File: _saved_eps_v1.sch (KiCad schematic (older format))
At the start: 8 parts

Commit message: Created netlist
Still missing deployment and RBL switches
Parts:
- removed U?: ATMEGA32M1-AU, TQFP32, symbol ATMEGA32M1-AU
- added C4, C5: 22pF, symbol C
- added U1: ATMEGA32M1-MU, QFN32, symbol ATMEGA32M1-MU
- added Y1: 8MHz, symbol Crystal_GND24
- gave numbers to parts that had none: 7
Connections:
- wire segments 16 -> 22
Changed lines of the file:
@@
 $EndDescr
 $Comp
-L switch S?
+L switch S1
 U 1 1 5998D4E2
 P 4700 4950
-F 0 "S?" H 4700 5100 60  0000 C CNN
+F 0 "S1" H 4700 5100 60  0000 C CNN
 F 1 "switch" H 4700 4900 60  0001 C CNN
 F 2 "" H 4700 4950 60  0001 C CNN
@@
 $EndComp
 $Comp
-L -BATT #PWR?
+L -BATT #PWR9
 U 1 1 5999015A
 P 4850 4950
-F 0 "#PWR?" H 4850 4800 50  0001 C CNN
+F 0 "#PWR9" H 4850 4800 50  0001 C CNN
 F 1 "-BATT" H 4850 5090 50  0000 C CNN
 F 2 "" H 4850 4950 50  0001 C CNN
@@
 $EndComp
 $Comp
-L switch S?
+L switch S2
 U 1 1 59990767
 P 4700 5400
-F 0 "S?" H 4700 5550 60  0000 C CNN
+F 0 "S2" H 4700 5550 60  0000 C CNN
 F 1 "switch" H 4700 5350 60  0001 C CNN
 F 2 "" H 4700 5400 60  0001 C CNN
@@
 $EndComp
 $Comp
-L switch S?
+L switch S3
 U 1 1 59990813
 P 4700 5750
-F 0 "S?" H 4700 5900 60  0000 C CNN
+F 0 "S3" H 4700 5900 60  0000 C CNN
 F 1 "switch" H 4700 5700 60  0001 C CNN
 F 2 "" H 4700 5750 60  0001 C CNN
@@
 $EndComp
 $Comp
-L +PACK #PWR?
+L +PACK #PWR5
 U 1 1 5999095F
 P 4550 5400
-F 0 "#PWR?" H 4550 5250 50  0001 C CNN
+F 0 "#PWR5" H 4550 5250 50  0001 C CNN
 F 1 "+PACK" H 4550 5540 50  0000 C CNN
 F 2 "" H 4550 5400 50  0001 C CNN
@@
 $EndComp
 $Comp
-L +BATT #PWR?
+L +BATT #PWR10
 U 1 1 599909D1
 P 4850 5750
-F 0 "#PWR?" H 4850 5600 50  0001 C CNN
+F 0 "#PWR10" H 4850 5600 50  0001 C CNN
 F 1 "+BATT" H 4850 5890 50  0000 C CNN
 F 2 "" H 4850 5750 50  0001 C CNN
@@
 $EndComp
 $Comp
-L switch S?
+L switch S4
 U 1 1 59990A70
 P 4750 4650
-F 0 "S?" H 4750 4800 60  0000 C CNN
+F 0 "S4" H 4750 4800 60  0000 C CNN
 F 1 "switch" H 4750 4600 60  0001 C CNN
 F 2 "" H 4750 4650 60  0001 C CNN
@@
 $EndComp
 $Comp
-L -PACK #PWR?
+L -PACK #PWR6
 U 1 1 59990B5A
 P 4600 4650
-F 0 "#PWR?" H 4600 4500 50  0001 C CNN
+F 0 "#PWR6" H 4600 4500 50  0001 C CNN
 F 1 "-PACK" H 4600 4790 50  0000 C CNN
 F 2 "" H 4600 4650 50  0001 C CNN
@@
 Text Notes 13600 1450 0    60   ~ 0
 Need to add the uC circuit (ATMEGA32M1)\nAdd all current and voltage sensors\ndecide whether to add the gas gauge (y) and the charging module (n)\nduplicate 3V3 supply and add a 12V supply
-$Comp
-L ATMEGA32M1-AU U?
-U 1 1 59D409BA
-P 6100 3000
-F 0 "U?" H 5150 4830 50  0000 L BNN
-F 1 "ATMEGA32M1-AU" H 6600 1600 50  0000 L BNN
-F 2 "TQFP32" H 6100 3000 50  0001 C CIN
-F 3 "" H 6100 3000 50  0001 C CNN
-	1    6100 3000
-	1    0    0    -1
-$EndComp
 $Sheet
 S 1550 6900 800  450
@@
 $EndSheet
 $Comp
-L GND #PWR?
+L GND #PWR11
 U 1 1 59EA5A22
 P 5000 4200
-F 0 "#PWR?" H 5000 3950 50  0001 C CNN
+F 0 "#PWR11" H 5000 3950 50  0001 C CNN
 F 1 "GND" H 5000 4050 50  0000 C CNN
 F 2 "" H 5000 4200 50  0001 C CNN
@@
 $EndComp
 $Comp
-L +3V3 #PWR?
+L +3V3 #PWR3
 U 1 1 59EA6A40
 P 4450 1300
-F 0 "#PWR?" H 4450 1150 50  0001 C CNN
+F 0 "#PWR3" H 4450 1150 50  0001 C CNN
 F 1 "+3V3" H 4450 1440 50  0000 C CNN
 F 2 "" H 4450 1300 50  0001 C CNN
@@
 $EndSheet
 $Sheet
-S 7850 3700 1000 1000
+S 8400 5100 1000 1000
 U 5A22FABC
 F0 "SWITCH_3V3" 60
 F1 "SWITCH_3V3.sch" 60
 $EndSheet
-Text HLabel 7850 3950 2    60   Input ~ 0
+Text HLabel 8400 5350 2    60   Input ~ 0
 3V3OUT
-Text HLabel 8850 3950 0    60   Output ~ 0
+Text HLabel 9400 5350 0    60   Output ~ 0
 N_3V3
-Text HLabel 7850 4200 2    60   Input ~ 0
+Text HLabel 8400 5600 2    60   Input ~ 0
 3V3_SWITCH
 $Sheet
@@
 Text HLabel 10650 2800 0    60   Output ~ 0
 E_9V
-Text HLabel 8850 4200 0    60   Output ~ 0
+Text HLabel 9400 5600 0    60   Output ~ 0
 E_3V3
 Text HLabel 9700 4850 2    60   Input ~ 0
@@
 Connection ~ 4750 1300
 $Comp
-L C C?
+L C C2
 U 1 1 5A75F62F
 P 4750 1050
-F 0 "C?" H 4775 1150 50  0000 L CNN
+F 0 "C2" H 4775 1150 50  0000 L CNN
 F 1 "0.1µF" H 4775 950 50  0000 L CNN
 F 2 "" H 4788 900 50  0001 C CNN
@@
 $EndComp
 $Comp
-L GND #PWR?
+L GND #PWR7
 U 1 1 5A75F783
 P 4750 900
-F 0 "#PWR?" H 4750 650 50  0001 C CNN
+F 0 "#PWR7" H 4750 650 50  0001 C CNN
 F 1 "GND" H 4750 750 50  0000 C CNN
 F 2 "" H 4750 900 50  0001 C CNN
@@
 $EndComp
 $Comp
-L +3V3 #PWR?
+L +3V3 #PWR1
 U 1 1 5A75F86F
 P 3600 1600
-F 0 "#PWR?" H 3600 1450 50  0001 C CNN
+F 0 "#PWR1" H 3600 1450 50  0001 C CNN
 F 1 "+3V3" H 3600 1740 50  0000 C CNN
 F 2 "" H 3600 1600 50  0001 C CNN
@@
 Connection ~ 3900 1600
 $Comp
-L C C?
+L C C1
 U 1 1 5A75F878
 P 3900 1350
-F 0 "C?" H 3925 1450 50  0000 L CNN
+F 0 "C1" H 3925 1450 50  0000 L CNN
 F 1 "0.1µF" H 3925 1250 50  0000 L CNN
 F 2 "" H 3938 1200 50  0001 C CNN
@@
 $EndComp
 $Comp
-L GND #PWR?
+L GND #PWR2
 U 1 1 5A75F87F
 P 3900 1200
-F 0 "#PWR?" H 3900 950 50  0001 C CNN
+F 0 "#PWR2" H 3900 950 50  0001 C CNN
 F 1 "GND" H 3900 1050 50  0000 C CNN
 F 2 "" H 3900 1200 50  0001 C CNN
@@
 $EndComp
 $Comp
-L +3V3 #PWR?
+L +3V3 #PWR4
 U 1 1 5A75F9CA
 P 4450 2000
-F 0 "#PWR?" H 4450 1850 50  0001 C CNN
+F 0 "#PWR4" H 4450 1850 50  0001 C CNN
 F 1 "+3V3" H 4450 2140 50  0000 C CNN
 F 2 "" H 4450 2000 50  0001 C CNN
@@
 Connection ~ 4750 2000
 $Comp
-L C C?
+L C C3
 U 1 1 5A75F9D3
 P 4750 2250
-F 0 "C?" H 4775 2350 50  0000 L CNN
+F 0 "C3" H 4775 2350 50  0000 L CNN
 F 1 "0.1µF" H 4775 2150 50  0000 L CNN
 F 2 "" H 4788 2100 50  0001 C CNN
@@
 $EndComp
 $Comp
-L GND #PWR?
+L GND #PWR8
 U 1 1 5A75F9DA
 P 4750 2400
-F 0 "#PWR?" H 4750 2150 50  0001 C CNN
+F 0 "#PWR8" H 4750 2150 50  0001 C CNN
 F 1 "GND" H 4750 2250 50  0000 C CNN
 F 2 "" H 4750 2400 50  0001 C CNN
@@
 	1    0    0    -1
 $EndComp
+$Comp
+L Crystal_GND24 Y1
+U 1 1 5A760437
+P 7850 4150
+F 0 "Y1" H 7975 4350 50  0000 L CNN
+F 1 "8MHz" H 7975 4275 50  0000 L CNN
+F 2 "" H 7850 4150 50  0001 C CNN
+F 3 "" H 7850 4150 50  0001 C CNN
+	1    7850 4150
+	0    1    1    0
+$EndComp
+Wire Wire Line
+	7400 4000 8400 4000
+Wire Wire Line
+	7400 4300 8400 4300
+$Comp
+L GND #PWR12
+U 1 1 5A7608B0
+P 7650 4150
+F 0 "#PWR12" H 7650 3900 50  0001 C CNN
+F 1 "GND" H 7650 4000 50  0000 C CNN
+F 2 "" H 7650 4150 50  0001 C CNN
+F 3 "" H 7650 4150 50  0001 C CNN
+	1    7650 4150
+	0    1    1    0
+$EndComp
+$Comp
+L GND #PWR13
+U 1 1 5A760948
+P 8050 4150
+F 0 "#PWR13" H 8050 3900 50  0001 C CNN
+F 1 "GND" H 8050 4000 50  0000 C CNN
+F 2 "" H 8050 4150 50  0001 C CNN
+F 3 "" H 8050 4150 50  0001 C CNN
+	1    8050 4150
+	0    -1   -1   0
+$EndComp
+Wire Wire Line
+	7400 4000 7400 4100
+Wire Wire Line
+	7400 4100 7200 4100
+Wire Wire Line
+	7400 4300 7400 4200
+Wire Wire Line
+	7400 4200 7200 4200
+$Comp
+L C C4
+U 1 1 5A760A5E
+P 8550 4000
+F 0 "C4" H 8575 4100 50  0000 L CNN
+F 1 "22pF" H 8575 3900 50  0000 L CNN
+F 2 "" H 8588 3850 50  0001 C CNN
+F 3 "" H 8550 4000 50  0001 C CNN
+	1    8550 4000
+	0    1    1    0
+$EndComp
+Connection ~ 7850 4000
+$Comp
+L C C5
+U 1 1 5A760D00
+P 8550 4300
+F 0 "C5" H 8575 4400 50  0000 L CNN
+F 1 "22pF" H 8575 4200 50  0000 L CNN
+F 2 "" H 8588 4150 50  0001 C CNN
+F 3 "" H 8550 4300 50  0001 C CNN
+	1    8550 4300
+	0    1    1    0
+$EndComp
+Connection ~ 7850 4300
+$Comp
+L GND #PWR14
+U 1 1 5A760E0D
+P 8700 4000
+F 0 "#PWR14" H 8700 3750 50  0001 C CNN
+F 1 "GND" H 8700 3850 50  0000 C CNN
+F 2 "" H 8700 4000 50  0001 C CNN
+F 3 "" H 8700 4000 50  0001 C CNN
+	1    8700 4000
+	0    -1   -1   0
+$EndComp
+$Comp
+L GND #PWR15
+U 1 1 5A760E69
+P 8700 4300
+F 0 "#PWR15" H 8700 4050 50  0001 C CNN
+F 1 "GND" H 8700 4150 50  0000 C CNN
+F 2 "" H 8700 4300 50  0001 C CNN
+F 3 "" H 8700 4300 50  0001 C CNN
+	1    8700 4300
+	0    -1   -1   0
+$EndComp
+$Comp
+L ATMEGA32M1-MU U1
+U 1 1 5A761CDE
+P 6100 3000
+F 0 "U1" H 5150 4830 50  0000 L BNN
+F 1 "ATMEGA32M1-MU" H 6600 1600 50  0000 L BNN
+F 2 "QFN32" H 6100 3000 50  0001 C CIN
+F 3 "" H 6100 3000 50  0001 C CNN
+	1    6100 3000
+	1    0    0    -1
+$EndComp

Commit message: hello
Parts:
- C1, C2, C3, C4, C5: footprint (none) -> Capacitors_SMD:C_0603_HandSoldering
- Y1: footprint (none) -> Housings_SOIC:SO-20_12.8x7.5mm_Pitch1.27mm
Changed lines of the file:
@@
 $EndComp
 $Comp
-L -BATT #PWR9
+L -BATT #PWR01
 U 1 1 5999015A
 P 4850 4950
-F 0 "#PWR9" H 4850 4800 50  0001 C CNN
+F 0 "#PWR01" H 4850 4800 50  0001 C CNN
 F 1 "-BATT" H 4850 5090 50  0000 C CNN
 F 2 "" H 4850 4950 50  0001 C CNN
@@
 $EndComp
 $Comp
-L +PACK #PWR5
+L +PACK #PWR02
 U 1 1 5999095F
 P 4550 5400
-F 0 "#PWR5" H 4550 5250 50  0001 C CNN
+F 0 "#PWR02" H 4550 5250 50  0001 C CNN
 F 1 "+PACK" H 4550 5540 50  0000 C CNN
 F 2 "" H 4550 5400 50  0001 C CNN
@@
 $EndComp
 $Comp
-L +BATT #PWR10
+L +BATT #PWR03
 U 1 1 599909D1
 P 4850 5750
-F 0 "#PWR10" H 4850 5600 50  0001 C CNN
+F 0 "#PWR03" H 4850 5600 50  0001 C CNN
 F 1 "+BATT" H 4850 5890 50  0000 C CNN
 F 2 "" H 4850 5750 50  0001 C CNN
@@
 $EndComp
 $Comp
-L -PACK #PWR6
+L -PACK #PWR04
 U 1 1 59990B5A
 P 4600 4650
-F 0 "#PWR6" H 4600 4500 50  0001 C CNN
+F 0 "#PWR04" H 4600 4500 50  0001 C CNN
 F 1 "-PACK" H 4600 4790 50  0000 C CNN
 F 2 "" H 4600 4650 50  0001 C CNN
@@
 $EndSheet
 $Comp
-L GND #PWR11
+L GND #PWR05
 U 1 1 59EA5A22
 P 5000 4200
-F 0 "#PWR11" H 5000 3950 50  0001 C CNN
+F 0 "#PWR05" H 5000 3950 50  0001 C CNN
 F 1 "GND" H 5000 4050 50  0000 C CNN
 F 2 "" H 5000 4200 50  0001 C CNN
@@
 $EndComp
 $Comp
-L +3V3 #PWR3
+L +3V3 #PWR06
 U 1 1 59EA6A40
 P 4450 1300
-F 0 "#PWR3" H 4450 1150 50  0001 C CNN
+F 0 "#PWR06" H 4450 1150 50  0001 C CNN
 F 1 "+3V3" H 4450 1440 50  0000 C CNN
 F 2 "" H 4450 1300 50  0001 C CNN
@@
 F 0 "C2" H 4775 1150 50  0000 L CNN
 F 1 "0.1µF" H 4775 950 50  0000 L CNN
-F 2 "" H 4788 900 50  0001 C CNN
+F 2 "Capacitors_SMD:C_0603_HandSoldering" H 4788 900 50  0001 C CNN
 F 3 "" H 4750 1050 50  0001 C CNN
 	1    4750 1050
@@
 $EndComp
 $Comp
-L GND #PWR7
+L GND #PWR07
 U 1 1 5A75F783
 P 4750 900
-F 0 "#PWR7" H 4750 650 50  0001 C CNN
+F 0 "#PWR07" H 4750 650 50  0001 C CNN
 F 1 "GND" H 4750 750 50  0000 C CNN
 F 2 "" H 4750 900 50  0001 C CNN
@@
 $EndComp
 $Comp
-L +3V3 #PWR1
+L +3V3 #PWR08
 U 1 1 5A75F86F
 P 3600 1600
-F 0 "#PWR1" H 3600 1450 50  0001 C CNN
+F 0 "#PWR08" H 3600 1450 50  0001 C CNN
 F 1 "+3V3" H 3600 1740 50  0000 C CNN
 F 2 "" H 3600 1600 50  0001 C CNN
@@
 F 0 "C1" H 3925 1450 50  0000 L CNN
 F 1 "0.1µF" H 3925 1250 50  0000 L CNN
-F 2 "" H 3938 1200 50  0001 C CNN
+F 2 "Capacitors_SMD:C_0603_HandSoldering" H 3938 1200 50  0001 C CNN
 F 3 "" H 3900 1350 50  0001 C CNN
 	1    3900 1350
@@
 $EndComp
 $Comp
-L GND #PWR2
+L GND #PWR09
 U 1 1 5A75F87F
 P 3900 1200
-F 0 "#PWR2" H 3900 950 50  0001 C CNN
+F 0 "#PWR09" H 3900 950 50  0001 C CNN
 F 1 "GND" H 3900 1050 50  0000 C CNN
 F 2 "" H 3900 1200 50  0001 C CNN
@@
 $EndComp
 $Comp
-L +3V3 #PWR4
+L +3V3 #PWR010
 U 1 1 5A75F9CA
 P 4450 2000
-F 0 "#PWR4" H 4450 1850 50  0001 C CNN
+F 0 "#PWR010" H 4450 1850 50  0001 C CNN
 F 1 "+3V3" H 4450 2140 50  0000 C CNN
 F 2 "" H 4450 2000 50  0001 C CNN
@@
 F 0 "C3" H 4775 2350 50  0000 L CNN
 F 1 "0.1µF" H 4775 2150 50  0000 L CNN
-F 2 "" H 4788 2100 50  0001 C CNN
+F 2 "Capacitors_SMD:C_0603_HandSoldering" H 4788 2100 50  0001 C CNN
 F 3 "" H 4750 2250 50  0001 C CNN
 	1    4750 2250
@@
 $EndComp
 $Comp
-L GND #PWR8
+L GND #PWR011
 U 1 1 5A75F9DA
 P 4750 2400
-F 0 "#PWR8" H 4750 2150 50  0001 C CNN
+F 0 "#PWR011" H 4750 2150 50  0001 C CNN
 F 1 "GND" H 4750 2250 50  0000 C CNN
 F 2 "" H 4750 2400 50  0001 C CNN
@@
 F 0 "Y1" H 7975 4350 50  0000 L CNN
 F 1 "8MHz" H 7975 4275 50  0000 L CNN
-F 2 "" H 7850 4150 50  0001 C CNN
+F 2 "Housings_SOIC:SO-20_12.8x7.5mm_Pitch1.27mm" H 7850 4150 50  0001 C CNN
 F 3 "" H 7850 4150 50  0001 C CNN
 	1    7850 4150
@@
 	7400 4300 8400 4300
 $Comp
-L GND #PWR12
+L GND #PWR012
 U 1 1 5A7608B0
 P 7650 4150
-F 0 "#PWR12" H 7650 3900 50  0001 C CNN
+F 0 "#PWR012" H 7650 3900 50  0001 C CNN
 F 1 "GND" H 7650 4000 50  0000 C CNN
 F 2 "" H 7650 4150 50  0001 C CNN
@@
 $EndComp
 $Comp
-L GND #PWR13
+L GND #PWR013
 U 1 1 5A760948
 P 8050 4150
-F 0 "#PWR13" H 8050 3900 50  0001 C CNN
+F 0 "#PWR013" H 8050 3900 50  0001 C CNN
 F 1 "GND" H 8050 4000 50  0000 C CNN
 F 2 "" H 8050 4150 50  0001 C CNN
@@
 F 0 "C4" H 8575 4100 50  0000 L CNN
 F 1 "22pF" H 8575 3900 50  0000 L CNN
-F 2 "" H 8588 3850 50  0001 C CNN
+F 2 "Capacitors_SMD:C_0603_HandSoldering" H 8588 3850 50  0001 C CNN
 F 3 "" H 8550 4000 50  0001 C CNN
 	1    8550 4000
@@
 F 0 "C5" H 8575 4400 50  0000 L CNN
 F 1 "22pF" H 8575 4200 50  0000 L CNN
-F 2 "" H 8588 4150 50  0001 C CNN
+F 2 "Capacitors_SMD:C_0603_HandSoldering" H 8588 4150 50  0001 C CNN
 F 3 "" H 8550 4300 50  0001 C CNN
 	1    8550 4300
@@
 Connection ~ 7850 4300
 $Comp
-L GND #PWR14
+L GND #PWR014
 U 1 1 5A760E0D
 P 8700 4000
-F 0 "#PWR14" H 8700 3750 50  0001 C CNN
+F 0 "#PWR014" H 8700 3750 50  0001 C CNN
 F 1 "GND" H 8700 3850 50  0000 C CNN
 F 2 "" H 8700 4000 50  0001 C CNN
@@
 $EndComp
 $Comp
-L GND #PWR15
+L GND #PWR015
 U 1 1 5A760E69
 P 8700 4300
-F 0 "#PWR15" H 8700 4050 50  0001 C CNN
+F 0 "#PWR015" H 8700 4050 50  0001 C CNN
 F 1 "GND" H 8700 4150 50  0000 C CNN
 F 2 "" H 8700 4300 50  0001 C CNN

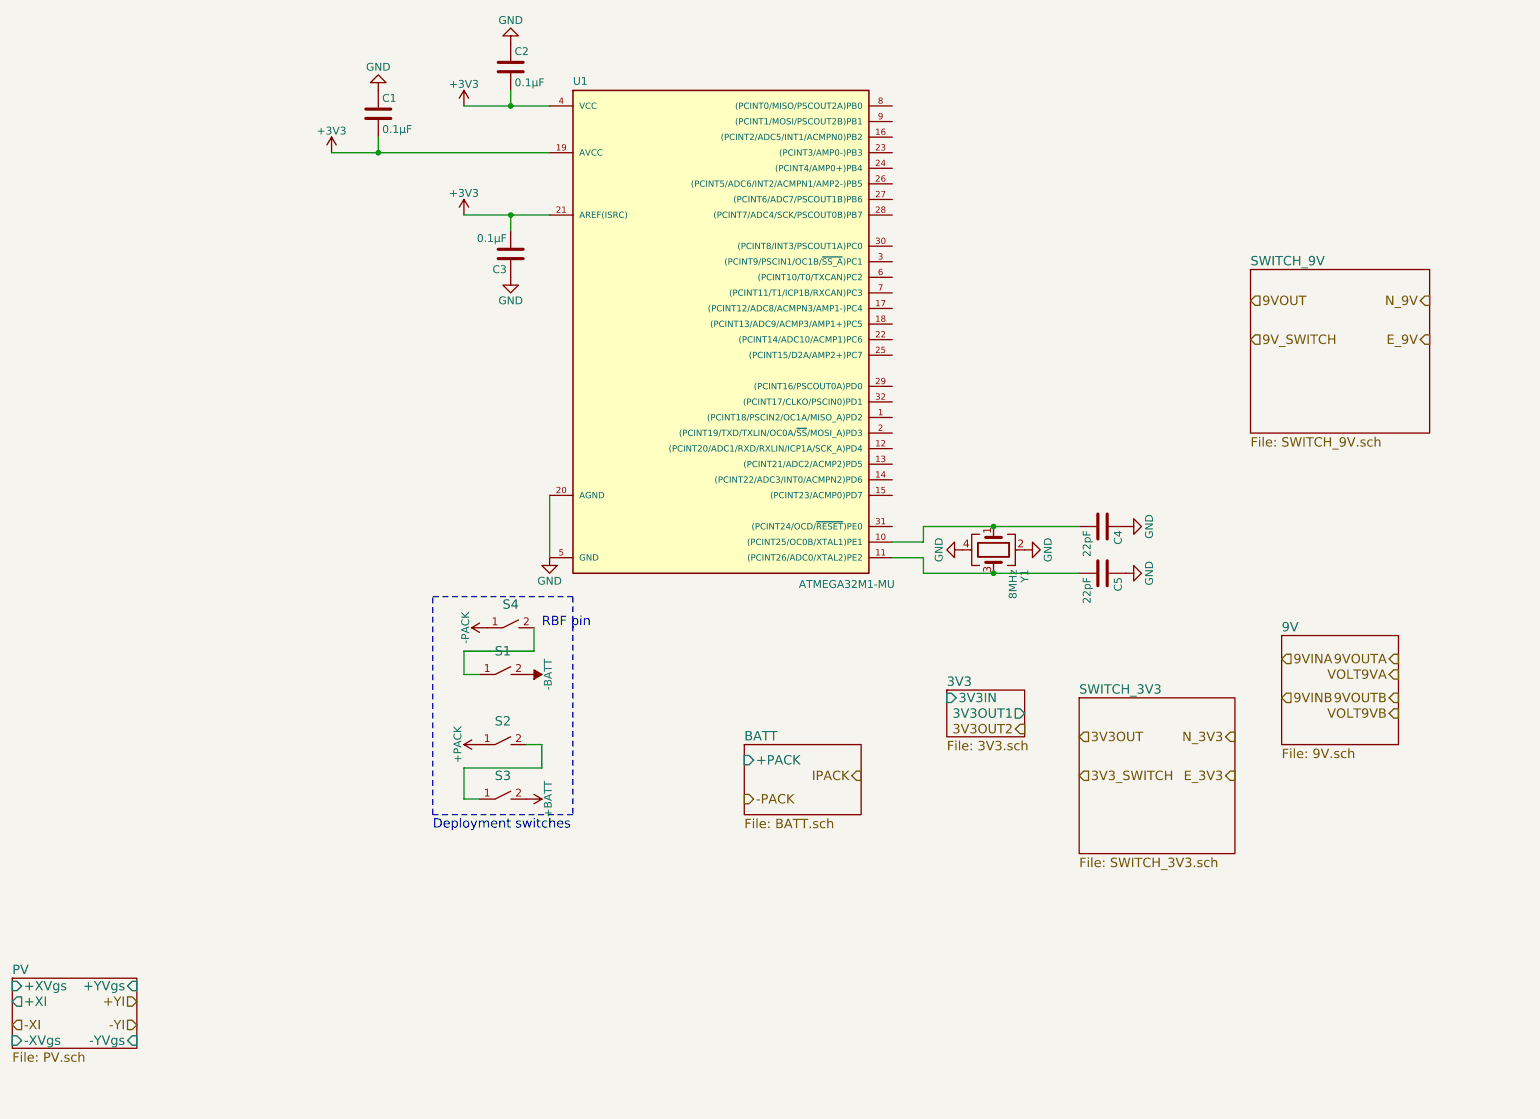
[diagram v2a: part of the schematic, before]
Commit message: Began interfacing with µC
Also all 9V should now be 5V, change resistors accordingly.
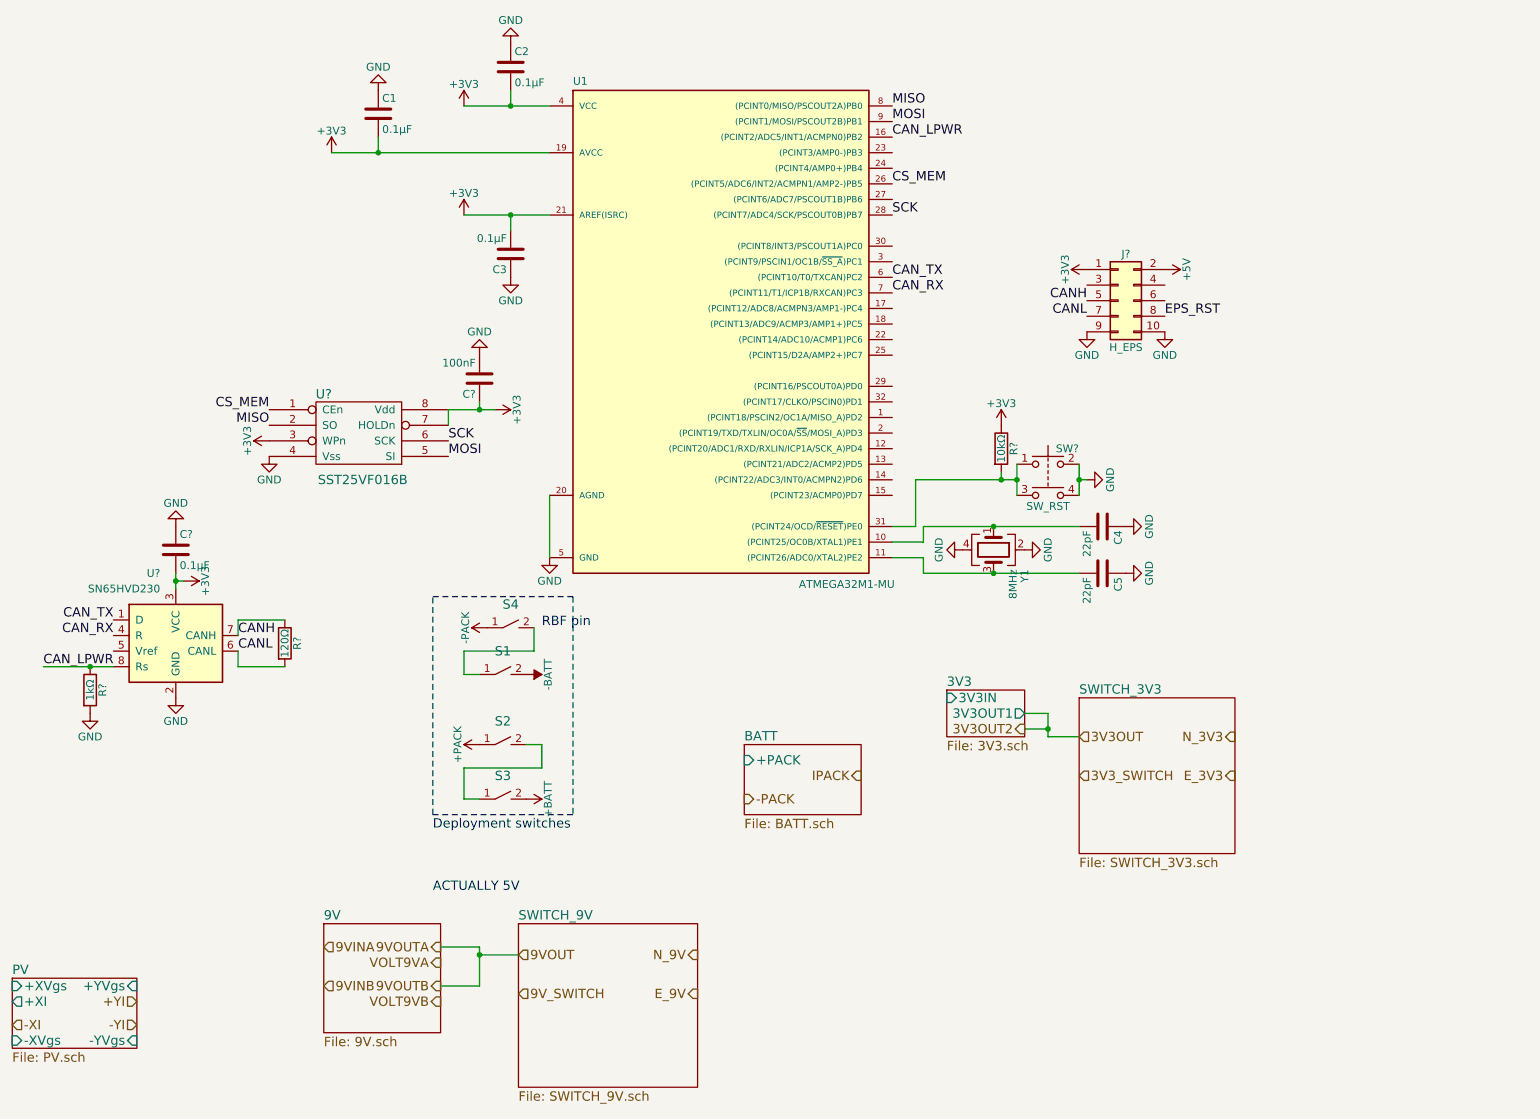
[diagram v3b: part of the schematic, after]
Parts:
- added C?: 0.1µF, symbol C
- added C?: 100nF, symbol C
- added J?: H_EPS, symbol Conn_02x05_Odd_Even
- added R?: 1kΩ, symbol R
- added R?: 120Ω, symbol R
- added R?: 10kΩ, symbol R
- added SW?: SW_RST, symbol SW_Push_Dual
- added U?: SN65HVD230, Housings_SOIC:SOIC-8_3.9x4.9mm_Pitch1.27mm, symbol SN65HVD230
- added U?: SST25VF016B, symbol SST25VF016B
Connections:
- net +3V3: now also C?.1, C?.2, J?.1 (Pin_1), R?.1, U?.3 (VCC), U?.3 (WPn), U?.7 (HOLDn), U?.8 (Vdd)
- net GND: now also C?.1, C?.2, J?.10 (Pin_10), J?.9 (Pin_9), R?.2, SW?.2, SW?.4, U?.2 (GND), U?.4 (Vss)
- net CAN_LPWR: now reaches U1.16 ((PCINT2/ADC5/INT1/ACMPN0)PB2)
- net CAN_LPWR: now also R?.1, U?.8 (Rs)
- net CS_MEM: now reaches U1.26 ((PCINT5/ADC6/INT2/ACMPN1/AMP2-)PB5)
- net CS_MEM: now also U?.1 (CEn)
- net SCK: now reaches U1.28 ((PCINT7/ADC4/SCK/PSCOUT0B)PB7)
- net SCK: now also U?.6 (SCK)
- net at U1.31 ((PCINT24/OCD/~RESET~)PE0): now also R?.2, SW?.1, SW?.3
- net CAN_TX: now reaches U1.6 ((PCINT10/T0/TXCAN)PC2)
- net CAN_TX: now also U?.1 (D)
- net CAN_RX: now reaches U1.7 ((PCINT11/T1/ICP1B/RXCAN)PC3)
- net CAN_RX: now also U?.4 (R)
- net MISO: now reaches U1.8 ((PCINT0/MISO/PSCOUT2A)PB0)
- net MISO: now also U?.2 (SO)
- net MOSI: now reaches U1.9 ((PCINT1/MOSI/PSCOUT2B)PB1)
- net MOSI: now also U?.5 (SI)
- new net +5V: J?.2 (Pin_2)
- new net CANH: J?.5 (Pin_5), R?.1, U?.7 (CANH)
- new net CANL: J?.7 (Pin_7), R?.2, U?.6 (CANL)
- new net EPS_RST: J?.8 (Pin_8)
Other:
- note added: "ACTUALLY 5V"

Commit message: PCB layout as of 2018-02-07
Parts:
- added J7: PROGRAMMING PORT, Pin_Headers:Pin_Header_Straight_2x03_Pitch2.54mm, symbol Conn_02x03_Odd_Even
- C6, C7: renamed from C?; footprint (none) -> Capacitors_SMD:C_0603_HandSoldering
- J8: renamed from J?; footprint (none) -> Pin_Headers:Pin_Header_Straight_2x05_Pitch2.54mm
- R5, R6, R7: renamed from R?; footprint (none) -> Resistors_SMD:R_0603_HandSoldering
- U1: footprint QFN32 -> Housings_DFN_QFN:QFN-32-1EP_7x7mm_Pitch0.65mm
- U8: renamed from U?; footprint Housings_SOIC:SOIC-8_3.9x4.9mm_Pitch1.27mm -> (none)
- U9: renamed from U?; footprint (none) -> kicad-libraries:SOIC8
- gave numbers to parts that had none: 1
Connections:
- net +3V3: now also J8.2 (Pin_2), J7.2 (Pin_2); no longer J8.1 (Pin_1)
- net +5V: now also J8.1 (Pin_1); no longer J8.2 (Pin_2)
- net CANH: now also J8.6 (Pin_6); no longer J8.5 (Pin_5)
- net CANL: now also J8.8 (Pin_8); no longer J8.7 (Pin_7)
- net EPS_RST: now also J8.7 (Pin_7); no longer J8.8 (Pin_8)
- net GND: now also J7.6 (Pin_6)
- net MISO_A: now reaches U1.1 ((PCINT18/PSCIN2/OC1A/MISO_A)PD2)
- net MISO_A: now also J7.1 (Pin_1)
- net SCK_A: now reaches U1.12 ((PCINT20/ADC1/RXD/RXLIN/ICP1A/SCK_A)PD4)
- net SCK_A: now also J7.3 (Pin_3)
- net MOSI_A: now reaches U1.2 ((PCINT19/TXD/TXLIN/OC0A/~SS~/MOSI_A)PD3)
- net MOSI_A: now also J7.4 (Pin_4)
- new net RST: J7.5 (Pin_5)
- no-connect marks 0 -> 4
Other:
- moved on the sheet: J8
